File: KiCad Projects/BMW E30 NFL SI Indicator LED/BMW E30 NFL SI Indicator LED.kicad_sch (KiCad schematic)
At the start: 14 parts, among them J1 Conn_01x12_Socket

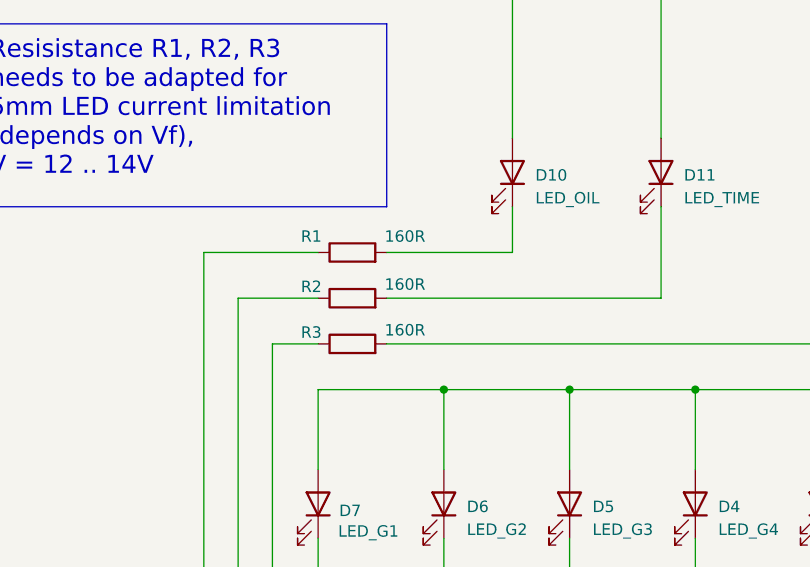
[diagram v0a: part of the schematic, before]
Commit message: Updated resistor values
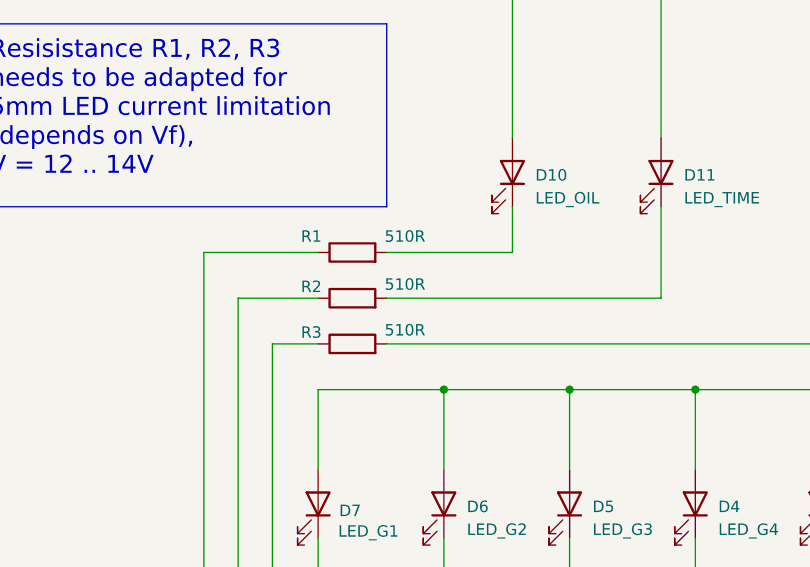
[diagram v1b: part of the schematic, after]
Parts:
- R1, R2, R3: value 160R -> 510R
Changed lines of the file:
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@@
 			)
 		)
-		(property "Value" "160R"
+		(property "Value" "510R"
 			(at 102.362 68.326 90)
 			(effects
@@
 			)
 		)
-		(property "Value" "160R"
+		(property "Value" "510R"
 			(at 102.362 73.406 90)
 			(effects
@@
 			)
 		)
-		(property "Value" "160R"
+		(property "Value" "510R"
 			(at 102.362 62.992 90)
 			(effects
